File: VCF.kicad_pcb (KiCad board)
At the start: 2 copper layers, 85 parts, among them J7 Conn_02x05_Odd_Even, U1 TL074, U2 TL074, U3 TL074, U4 LM13700, U5 LM13700, U6 LM13700

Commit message: Partial placement.
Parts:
- moved R6 120.2 mm to (43.2, 63.6), turned to 180 degrees
- moved R10 116.5 mm to (43.2, 58.7), turned to 180 degrees
- moved R30 110.4 mm to (51.9, 40.4), turned to 90 degrees
- moved R25 109.4 mm to (47.2, 40.3), turned to 90 degrees
- moved R31 109.0 mm to (50.5, 48.5), turned to 270 degrees
- moved R33 107.9 mm to (56.3, 40.5), turned to 90 degrees
- moved R29 104.8 mm to (54.4, 48.5), turned to 90 degrees
- moved R27 103.6 mm to (54.4, 44.8), turned to 270 degrees
- moved R20 101.7 mm to (61.3, 70.6), turned to 180 degrees
- moved R9 101.1 mm to (55.5, 58.8)
- moved R17 100.4 mm to (61.1, 54.5)
- moved R26 100.3 mm to (61.2, 40.4), turned to 270 degrees
- moved C5 99.7 mm to (58.8, 46.6), turned to 90 degrees
- moved R2 99.0 mm to (43.2, 61.1)
- moved R14 95.4 mm to (61.3, 67.8)
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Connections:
- C1 pad 2: GND -> (no net)
- C10 pad 2: GND -> (no net)
- C11 pad 2: GND -> (no net)
- C12 pad 2: GND -> (no net)
- C13 pad 2: GND -> (no net)
- C14 pad 2: GND -> (no net)
- C15 pad 2: GND -> (no net)
- C16 pad 1: GND -> (no net)
- C17 pad 1: GND -> (no net)
- C18 pad 1: GND -> (no net)
- C19 pad 1: GND -> (no net)
- C2 pad 2: GND -> (no net)
- C20 pad 1: GND -> (no net)
- C21 pad 1: GND -> (no net)
- C22 pad 1: GND -> (no net)
- C3 pad 2: GND -> (no net)
- C4 pad 2: GND -> (no net)
- C9 pad 2: GND -> (no net)
- J7 pad 3: GND -> (no net)
- J7 pad 4: GND -> (no net)
- J7 pad 5: GND -> (no net)
- J7 pad 6: GND -> (no net)
- J7 pad 7: GND -> (no net)
- J7 pad 8: GND -> (no net)
- R18 pad 2: GND -> (no net)
- R20 pad 2: GND -> (no net)
- R22 pad 2: GND -> (no net)
- R24 pad 2: GND -> (no net)
- R32 pad 2: GND -> (no net)
- R36 pad 2: GND -> (no net)
- R37 pad 1: GND -> (no net)
- R52 pad 2: GND -> (no net)
- R53 pad 1: GND -> (no net)
- R55 pad 2: GND -> (no net)
- R56 pad 2: GND -> (no net)
- U1 pad 10: GND -> (no net)
- U1 pad 3: GND -> (no net)
- U1 pad 5: GND -> (no net)
- U3 pad 10: GND -> (no net)
- U3 pad 12: GND -> (no net)
- U3 pad 3: GND -> (no net)
- U4 pad 14: GND -> (no net)
- U4 pad 3: GND -> (no net)
- U5 pad 14: GND -> (no net)
- U5 pad 3: GND -> (no net)
- U6 pad 13: GND -> (no net)
- U6 pad 3: GND -> (no net)
- U6 pad 4: GND -> (no net)

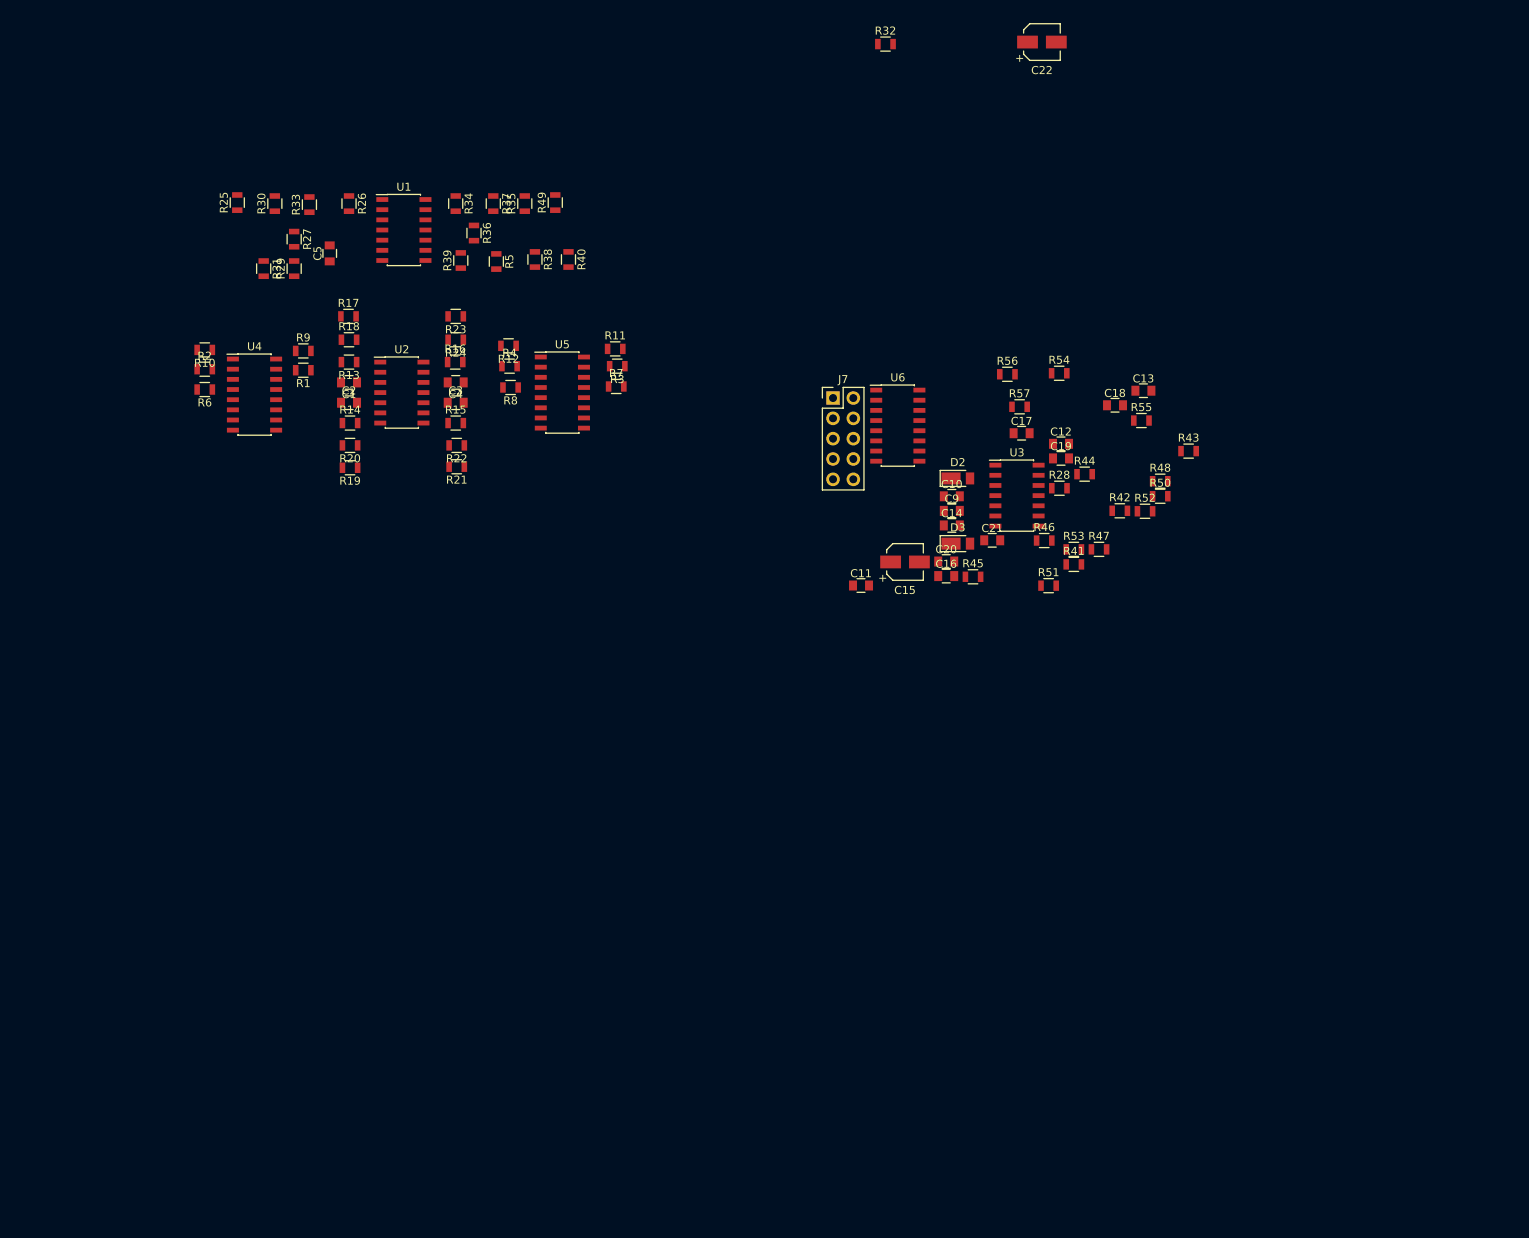
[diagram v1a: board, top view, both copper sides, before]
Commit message: More footprints and placement.
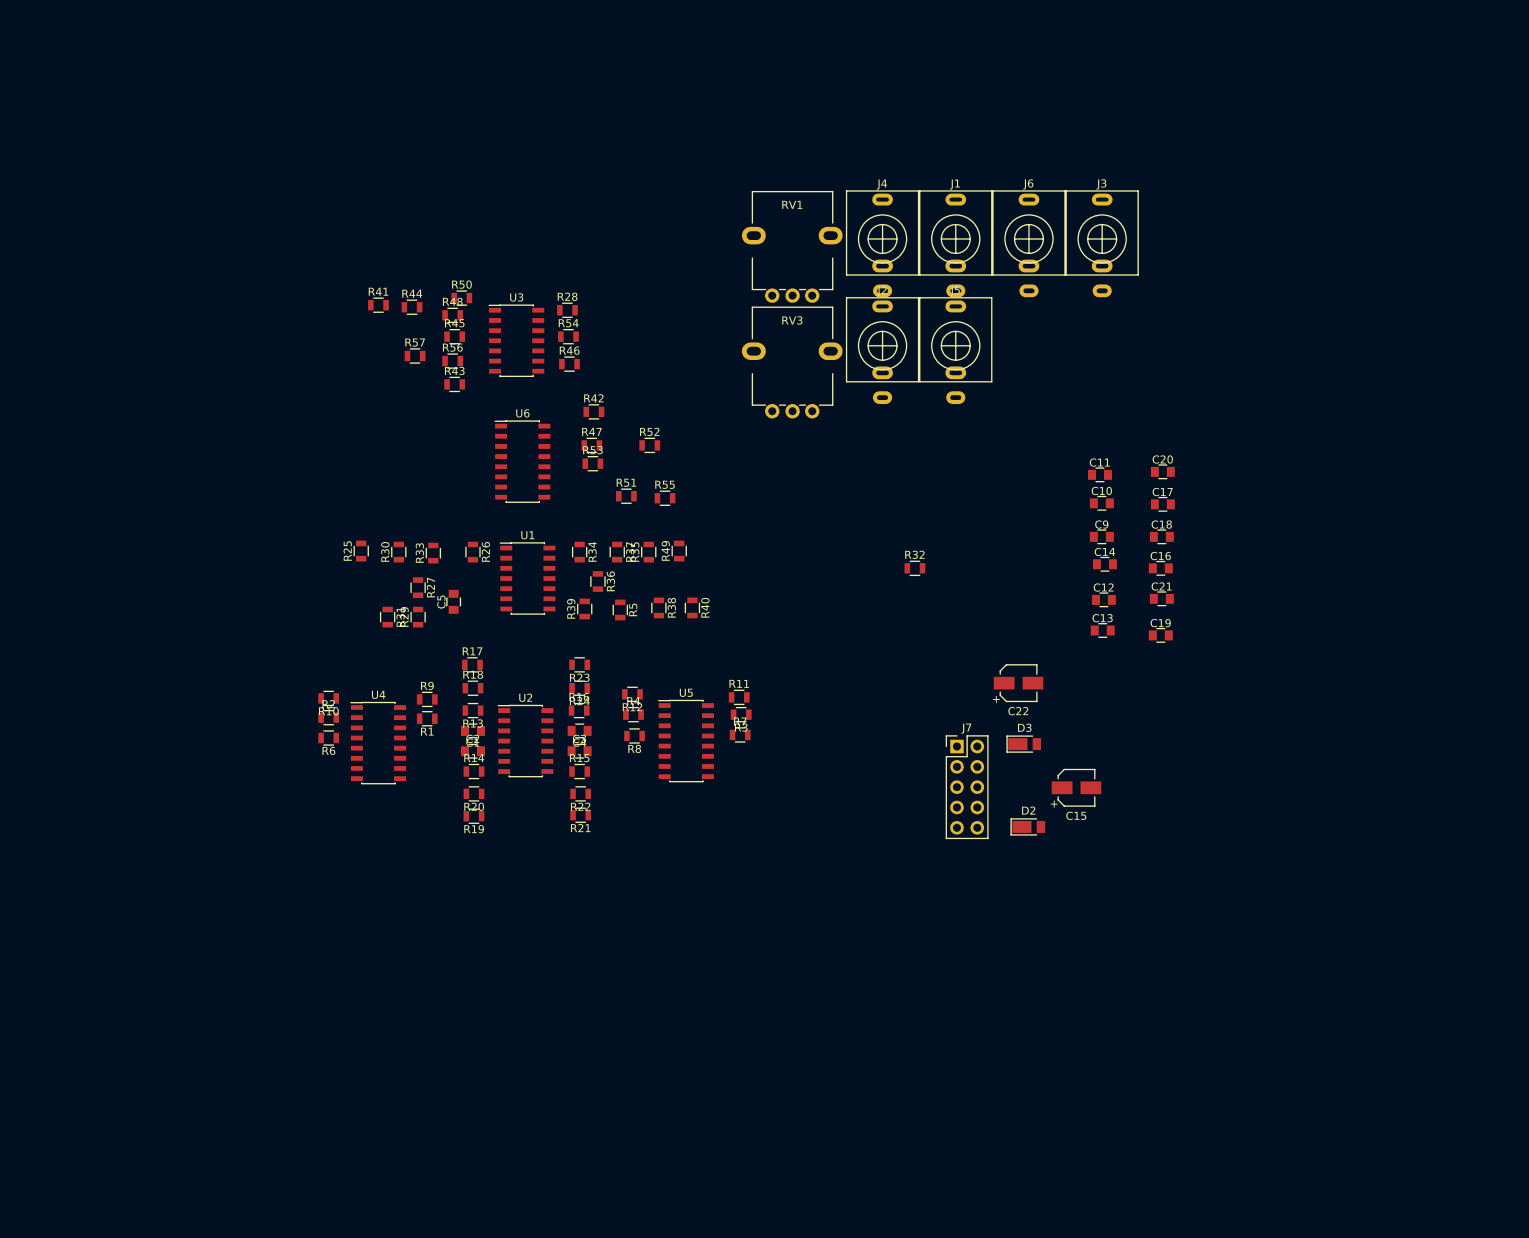
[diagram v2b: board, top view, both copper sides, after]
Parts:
- added J1: AudioJack2_Ground_Switch, Local:PJ398SM, F.Cu at (137.1, 44.8)
- added J2: AudioJack2_Ground_Switch, Local:PJ398SM, F.Cu at (127.9, 58.2)
- added J3: AudioJack2_Ground_Switch, Local:PJ398SM, F.Cu at (155.4, 44.8)
- added J4: AudioJack2_Ground_Switch, Local:PJ398SM, F.Cu at (127.9, 44.8)
- added J5: AudioJack2_Ground_Switch, Local:PJ398SM, F.Cu at (137.1, 58.2)
- added J6: AudioJack2_Ground_Switch, Local:PJ398SM, F.Cu at (146.2, 44.8)
- added RV1: 100k, Local:AlpsRK09K, F.Cu at (116.6, 44.4)
- added RV3: 100k, Local:AlpsRK09K, F.Cu at (116.6, 58.8)
- moved R41 92.8 mm to (64.9, 53.1)
- moved R43 92.1 mm to (74.4, 63.0)
- moved R48 90.8 mm to (74.2, 54.4)
- moved R50 90.7 mm to (75.3, 52.2)
- moved R44 86.6 mm to (69.1, 53.3)
- moved C22 80.2 mm to (144.9, 100.3)
- moved R57 75.8 mm to (69.5, 59.4)
- moved R45 71.4 mm to (74.4, 57.0)
- moved R56 69.4 mm to (74.2, 60.1)
- moved R42 66.9 mm to (91.8, 66.4)
- moved R32 65.6 mm to (132.0, 86.0)
- moved U3 65.5 mm to (82.2, 57.5)
- moved R28 65.4 mm to (88.5, 53.7)
- moved R47 64.7 mm to (91.6, 70.6)
- moved R46 63.3 mm to (88.8, 60.5)
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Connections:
- C1 pad 2: (no net) -> GND
- C10 pad 2: (no net) -> GND
- C11 pad 2: (no net) -> GND
- C12 pad 2: (no net) -> GND
- C13 pad 2: (no net) -> GND
- C14 pad 2: (no net) -> GND
- C15 pad 2: (no net) -> GND
- C16 pad 1: (no net) -> GND
- C17 pad 1: (no net) -> GND
- C18 pad 1: (no net) -> GND
- C19 pad 1: (no net) -> GND
- C2 pad 2: (no net) -> GND
- C20 pad 1: (no net) -> GND
- C21 pad 1: (no net) -> GND
- C22 pad 1: (no net) -> GND
- C3 pad 2: (no net) -> GND
- C4 pad 2: (no net) -> GND
- C9 pad 2: (no net) -> GND
- J7 pad 3: (no net) -> GND
- J7 pad 4: (no net) -> GND
- J7 pad 5: (no net) -> GND
- J7 pad 6: (no net) -> GND
- J7 pad 7: (no net) -> GND
- J7 pad 8: (no net) -> GND
- R18 pad 2: (no net) -> GND
- R20 pad 2: (no net) -> GND
- R22 pad 2: (no net) -> GND
- R24 pad 2: (no net) -> GND
- R32 pad 2: (no net) -> GND
- R36 pad 2: (no net) -> GND
- R37 pad 1: (no net) -> GND
- R52 pad 2: (no net) -> GND
- R53 pad 1: (no net) -> GND
- R55 pad 2: (no net) -> GND
- R56 pad 2: (no net) -> GND
- U1 pad 10: (no net) -> GND
- U1 pad 3: (no net) -> GND
- U1 pad 5: (no net) -> GND
- U3 pad 10: (no net) -> GND
- U3 pad 12: (no net) -> GND
- U3 pad 3: (no net) -> GND
- U4 pad 14: (no net) -> GND
- U4 pad 3: (no net) -> GND
- U5 pad 14: (no net) -> GND
- U5 pad 3: (no net) -> GND
- U6 pad 13: (no net) -> GND
- U6 pad 3: (no net) -> GND
- U6 pad 4: (no net) -> GND

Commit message: More work on layout.
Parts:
- added C6: 100n, Capacitors_THT:C_Rect_L7.2mm_W2.5mm_P5.00mm_FKS2_FKP2_MKS2_MKP2, F.Cu at (182.5, 93.8)
- added C7: 470n, Capacitors_THT:C_Rect_L7.2mm_W3.5mm_P5.00mm_FKS2_FKP2_MKS2_MKP2, F.Cu at (174.6, 94.3)
- added C8: 470n, Capacitors_THT:C_Rect_L7.2mm_W3.5mm_P5.00mm_FKS2_FKP2_MKS2_MKP2, F.Cu at (184.7, 88.9)
- added D1: 1N4148, Diodes_SMD:D_SOD-123F, F.Cu at (66.0, 87.8)
- added Q1: BC857, TO_SOT_Packages_SMD:SOT-23, F.Cu at (139.8, 77.7)
- added Q2: BC857, TO_SOT_Packages_SMD:SOT-23, F.Cu at (143.2, 74.2)
- added Q3: BC857, TO_SOT_Packages_SMD:SOT-23, F.Cu at (139.8, 74.2)
- added Q4: BC857, TO_SOT_Packages_SMD:SOT-23, F.Cu at (136.3, 77.7)
- added Q5: BC847, TO_SOT_Packages_SMD:SOT-23, F.Cu at (136.3, 74.2)
- added Q6: BC847, TO_SOT_Packages_SMD:SOT-23, F.Cu at (143.2, 77.7)
- added RV2: 100, Potentiometers:Potentiometer_Trimmer_Bourns_3296W, F.Cu at (180.7, 89.5)
- added RV4: 100k, Local:AlpsRK09K, F.Cu at (166.4, 58.4)
- added RV5: 100k, Local:AlpsRK09K, F.Cu at (179.8, 58.4)

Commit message: More developement work.
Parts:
- C1, C10, C11, C12, C13, C14, C16, C17, C18, C19, C2, C20, C21, C3, C4, C5, C9: footprint Capacitors_SMD:C_0805 -> Capacitor_SMD:C_0603_1608Metric
- C6: footprint Capacitors_THT:C_Rect_L7.2mm_W2.5mm_P5.00mm_FKS2_FKP2_MKS2_MKP2 -> Capacitor_SMD:C_0805_2012Metric
- C7, C8: footprint Capacitors_THT:C_Rect_L7.2mm_W3.5mm_P5.00mm_FKS2_FKP2_MKS2_MKP2 -> Capacitor_SMD:C_1206_3216Metric
- R1, R10, R11, R12, R13, R14, R15, R16, R17, R18, R19, R2, R20, R21, R22, R23, R24, R25, R26, R27, R28, R29, R3, R30, R31, R32, R33, R34, R35, R36, R37, R38, R39, R4, R40, R41, R42, R43, R44, R45, R46, R47, R48, R49, R5, R50, R51, R52, R53, R54, R55, R56, R57, R6, R7, R8, R9: footprint Resistors_SMD:R_0805 -> Resistor_SMD:R_0603_1608Metric
- moved C6 123.0 mm to (65.2, 130.4)
- moved C8 119.8 mm to (70.1, 123.7)
- moved C16 117.0 mm to (55.9, 133.9)
- moved C19 117.0 mm to (55.9, 142.2)
- moved C22 117.0 mm to (38.1, 148.2)
- moved D3 117.0 mm to (38.9, 155.8)
- moved Q1 117.0 mm to (33.0, 125.6)
- moved Q3 117.0 mm to (33.0, 122.0)
- moved C10 117.0 mm to (48.5, 125.7)
- moved C11 117.0 mm to (48.3, 122.2)
- moved C13 117.0 mm to (48.6, 141.6)
- moved C17 117.0 mm to (56.1, 125.9)
- moved C21 117.0 mm to (56.0, 137.7)
- moved D2 117.0 mm to (39.4, 166.2)
- moved Q2 117.0 mm to (36.4, 122.0)
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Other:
- board outline added: 39.6 x 100 mm
